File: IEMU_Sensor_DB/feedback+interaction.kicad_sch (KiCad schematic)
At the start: 29 parts, among them J301 +, J302 -, M401 VZ43FM1B8230001L, Q301 CSD13381F4, Q302 CSD13381F4, Q303 CSD13381F4, Q304 CSD13381F4, SW301 NANOT_160_BP, SW302 TS-1088-AR02016

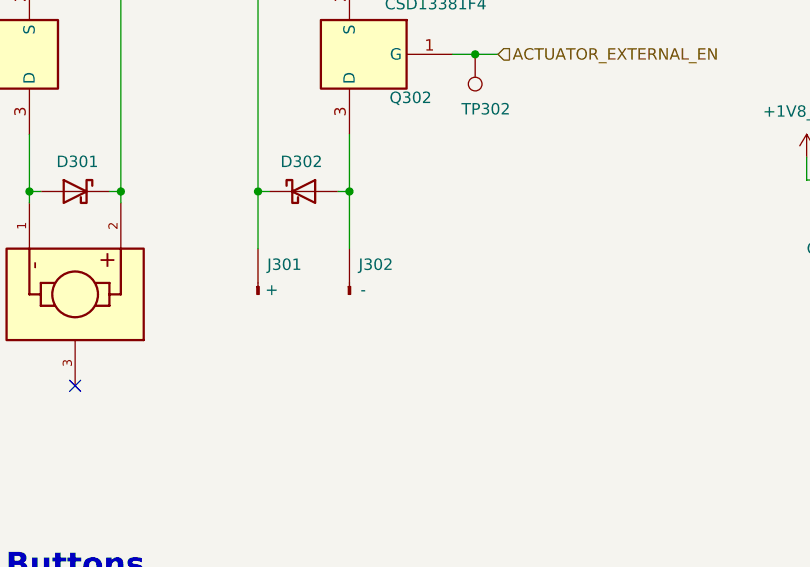
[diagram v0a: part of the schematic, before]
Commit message: swapped the coin cell vibration actuator pins
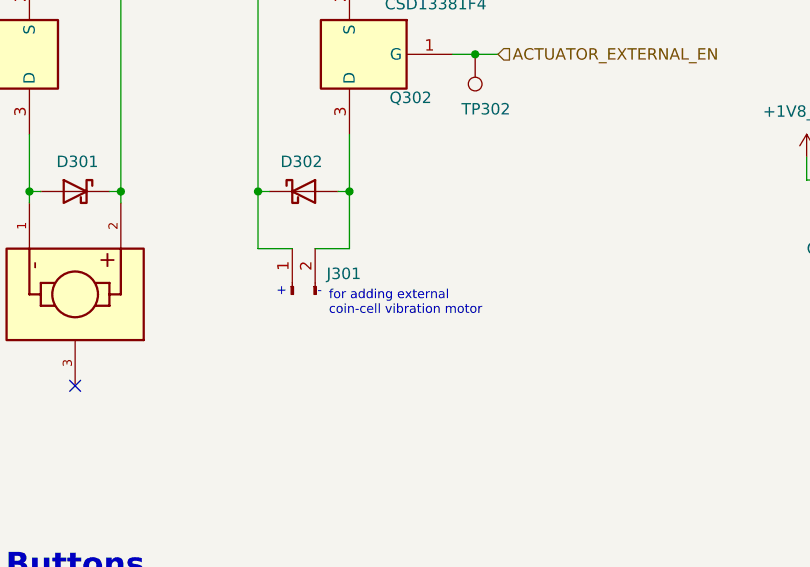
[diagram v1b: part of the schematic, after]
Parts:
- removed J301: +, 0_Connectors:Edge_Header_Pin, symbol 0_Connectors:Connector_Pin_Header_Edge
- removed J302: -, 0_Connectors:Edge_Header_Pin, symbol 0_Connectors:Connector_Pin_Header_Edge
- added J301: Conn_01x02_Pin, Connector_Wire:SolderWire-0.5sqmm_1x02_P4.6mm_D0.9mm_OD2.1mm, symbol Connector:Conn_01x02_Pin
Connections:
- net +3V0: now also J301.1 (Pin_1)
- net at D302.2 (A), Q302.3 (D): now also J301.2 (Pin_2)
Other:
- note added: "+"
- note added: "-"
- note added: "for adding external coin-cell vibration motor"
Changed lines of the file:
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@@
 		)
 	)
+	(text "+"
+		(exclude_from_sim no)
+		(at 82.042 115.316 0)
+		(effects
+			(font
+				(size 1.016 1.016)
+			)
+			(justify left)
+		)
+	)
 	(text "Actuators, LEDs & Buttons"
 		(exclude_from_sim no)
@@
 		)
 	)
+	(text "-"
+		(exclude_from_sim no)
+		(at 86.614 115.316 0)
+		(effects
+			(font
+				(size 1.016 1.016)
+			)
+			(justify left)
+		)
+	)
 	(text "+VSYS Rail"
 		(exclude_from_sim no)
@@
 		)
 	)
+	(text "for adding external \ncoin-cell vibration motor"
+		(exclude_from_sim no)
+		(at 87.884 116.586 0)
+		(effects
+			(font
+				(size 1.016 1.016)
+			)
+			(justify left)
+		)
+	)
 	(text "Haptic Actuators"
 		(exclude_from_sim no)
@@
 	(wire
 		(pts
+			(xy 86.36 110.49) (xy 90.17 110.49)
+		)
+		(stroke
+			(width 0)
+			(type default)
+		)
+	)
+	(wire
+		(pts
 			(xy 140.97 102.87) (xy 140.97 100.33)
 		)
@@
 	(wire
 		(pts
+			(xy 80.01 110.49) (xy 83.82 110.49)
+		)
+		(stroke
+			(width 0)
+			(type default)
+		)
+	)
+	(wire
+		(pts
 			(xy 237.49 67.31) (xy 237.49 72.39)
 		)
@@
 	)
 	(symbol
-		(lib_name "Connector_Pin_Header_Edge_1")
-		(lib_id "0_Connectors:Connector_Pin_Header_Edge")
-		(at 80.01 115.57 90)
-		(unit 1)
-		(exclude_from_sim no)
-		(in_bom yes)
-		(on_board yes)
-		(dnp no)
-		(property "Reference" "J301"
-			(at 81.026 112.268 90)
-			(effects
-				(font
-					(size 1.27 1.27)
-				)
-				(justify right)
-			)
-		)
-		(property "Value" "+"
-			(at 81.534 115.062 90)
-			(effects
-				(font
-					(size 1.27 1.27)
-				)
-			)
-		)
-		(property "Footprint" "0_Connectors:Edge_Header_Pin"
-			(at 81.534 115.57 0)
-			(effects
-				(font
-					(size 1.27 1.27)
-				)
-				(hide yes)
-			)
-		)
-		(property "Datasheet" ""
-			(at 85.852 115.57 0)
-			(effects
-				(font
-					(size 1.27 1.27)
-				)
-				(hide yes)
-			)
-		)
-		(property "Description" "Header Pin located on the edge of the board"
-			(at 84.074 115.316 0)
-			(effects
-				(font
-					(size 1.27 1.27)
-				)
-				(hide yes)
-			)
-		)
-		(pin "1"
-		)
-		(instances
-			(project "IEMU"
-				(path "/114b31f2-6a4f-42ef-aa97-5a200e091126/bedc77cc-dda1-48b8-87d2-cdf0a97ca477"
-					(reference "J301")
-					(unit 1)
-				)
-			)
-		)
-	)
-	(symbol
 		(lib_id "0_Feedback:TS-1088-AR02016")
 		(at 113.03 160.02 0)
@@
 	)
 	(symbol
-		(lib_id "0_Connectors:Connector_Pin_Header_Edge")
-		(at 90.17 115.57 90)
-		(unit 1)
-		(exclude_from_sim no)
-		(in_bom yes)
-		(on_board yes)
-		(dnp no)
-		(property "Reference" "J302"
-			(at 91.186 112.268 90)
-			(effects
-				(font
-					(size 1.27 1.27)
-				)
-				(justify right)
-			)
-		)
-		(property "Value" "-"
-			(at 91.694 115.062 90)
-			(effects
-				(font
-					(size 1.27 1.27)
-				)
-			)
-		)
-		(property "Footprint" "0_Connectors:Edge_Header_Pin"
-			(at 91.694 115.57 0)
-			(effects
-				(font
-					(size 1.27 1.27)
-				)
-				(hide yes)
-			)
-		)
-		(property "Datasheet" ""
-			(at 96.012 115.57 0)
-			(effects
-				(font
-					(size 1.27 1.27)
-				)
-				(hide yes)
-			)
-		)
-		(property "Description" "Header Pin located on the edge of the board"
-			(at 94.234 115.316 0)
-			(effects
-				(font
-					(size 1.27 1.27)
-				)
-				(hide yes)
-			)
-		)
-		(pin "1"
-		)
-		(instances
-			(project ""
-				(path "/114b31f2-6a4f-42ef-aa97-5a200e091126/bedc77cc-dda1-48b8-87d2-cdf0a97ca477"
-					(reference "J302")
-					(unit 1)
-				)
-			)
-		)
-	)
-	(symbol
 		(lib_id "Connector:TestPoint")
 		(at 52.07 161.29 0)
@@
 					(unit 1)
 				)
+			)
+		)
+	)
+	(symbol
+		(lib_id "Connector:Conn_01x02_Pin")
+		(at 83.82 115.57 90)
+		(unit 1)
+		(exclude_from_sim no)
+		(in_bom no)
+		(on_board yes)
+		(dnp no)
+		(property "Reference" "J301"
+			(at 87.63 113.284 90)
+			(effects
+				(font
+					(size 1.27 1.27)
+				)
+				(justify right)
+			)
+		)
+		(property "Value" "Conn_01x02_Pin"
+			(at 87.63 116.2049 90)
+			(effects
+				(font
+					(size 1.27 1.27)
+				)
+				(justify right)
+				(hide yes)
+			)
+		)
+		(property "Footprint" "Connector_Wire:SolderWire-0.5sqmm_1x02_P4.6mm_D0.9mm_OD2.1mm"
+			(at 83.82 115.57 0)
+			(effects
+				(font
+					(size 1.27 1.27)
+				)
+				(hide yes)
+			)
+		)
+		(property "Datasheet" "~"
+			(at 83.82 115.57 0)
+			(effects
+				(font
+					(size 1.27 1.27)
+				)
+				(hide yes)
+			)
+		)
+		(property "Description" "Generic connector, single row, 01x02, script generated"
+			(at 83.82 115.57 0)
+			(effects
+				(font
+					(size 1.27 1.27)
+				)
+				(hide yes)
+			)
+		)
+		(pin "2"
+		)
+		(pin "1"
+		)
+		(instances
+			(project ""
+				(path "/114b31f2-6a4f-42ef-aa97-5a200e091126/bedc77cc-dda1-48b8-87d2-cdf0a97ca477"
+					(reference "J301")
+					(unit 1)
+				)

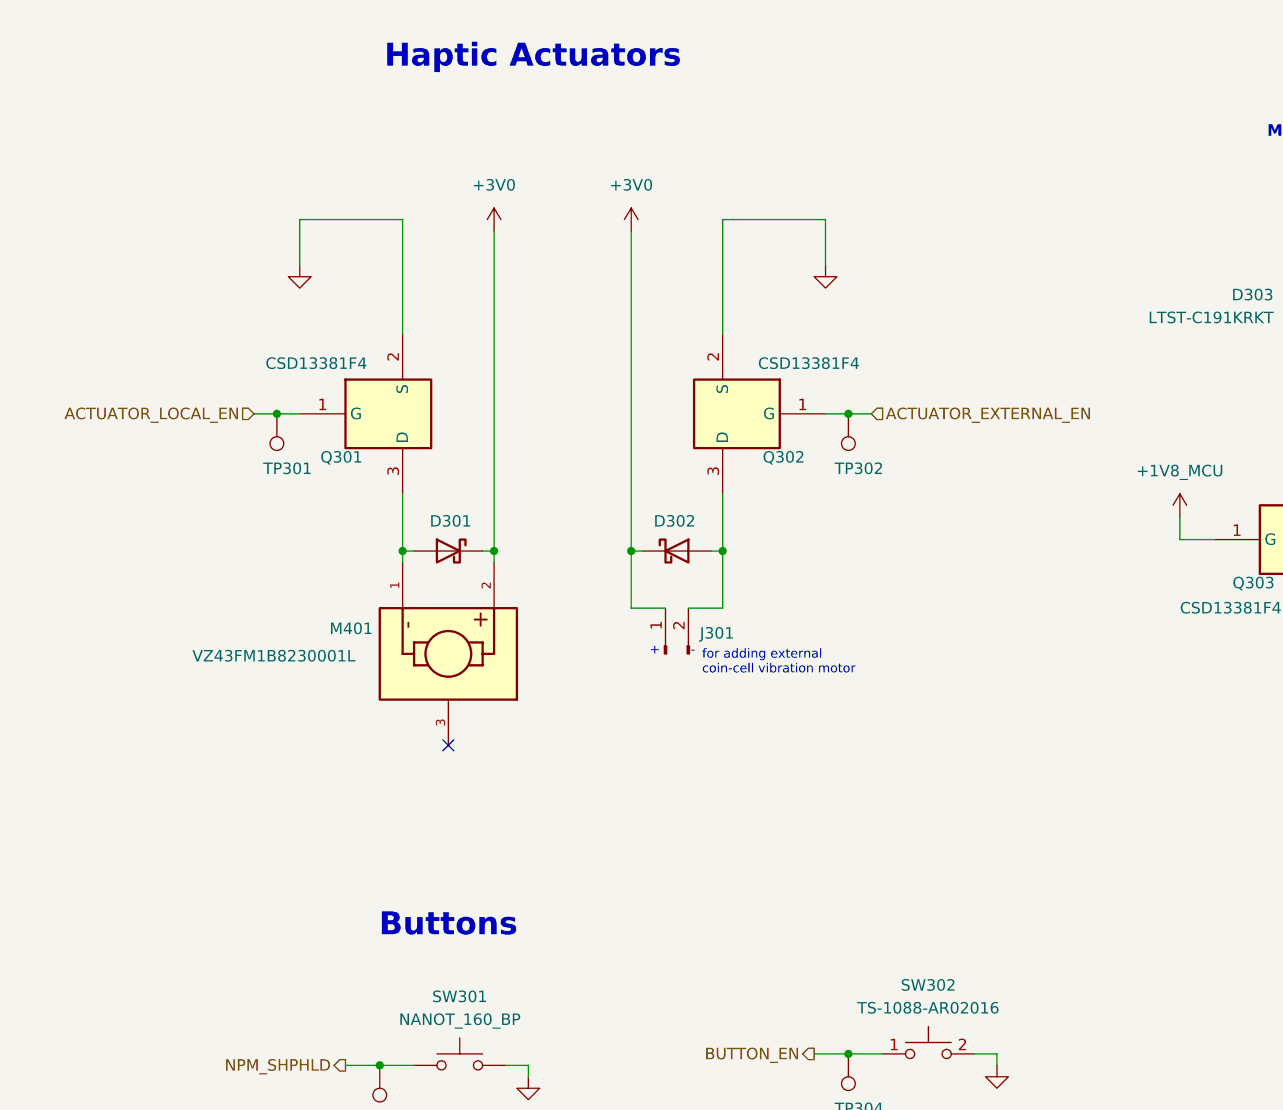
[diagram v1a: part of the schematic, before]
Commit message: implemented changes from the review with TF and fixed lost parts in the library
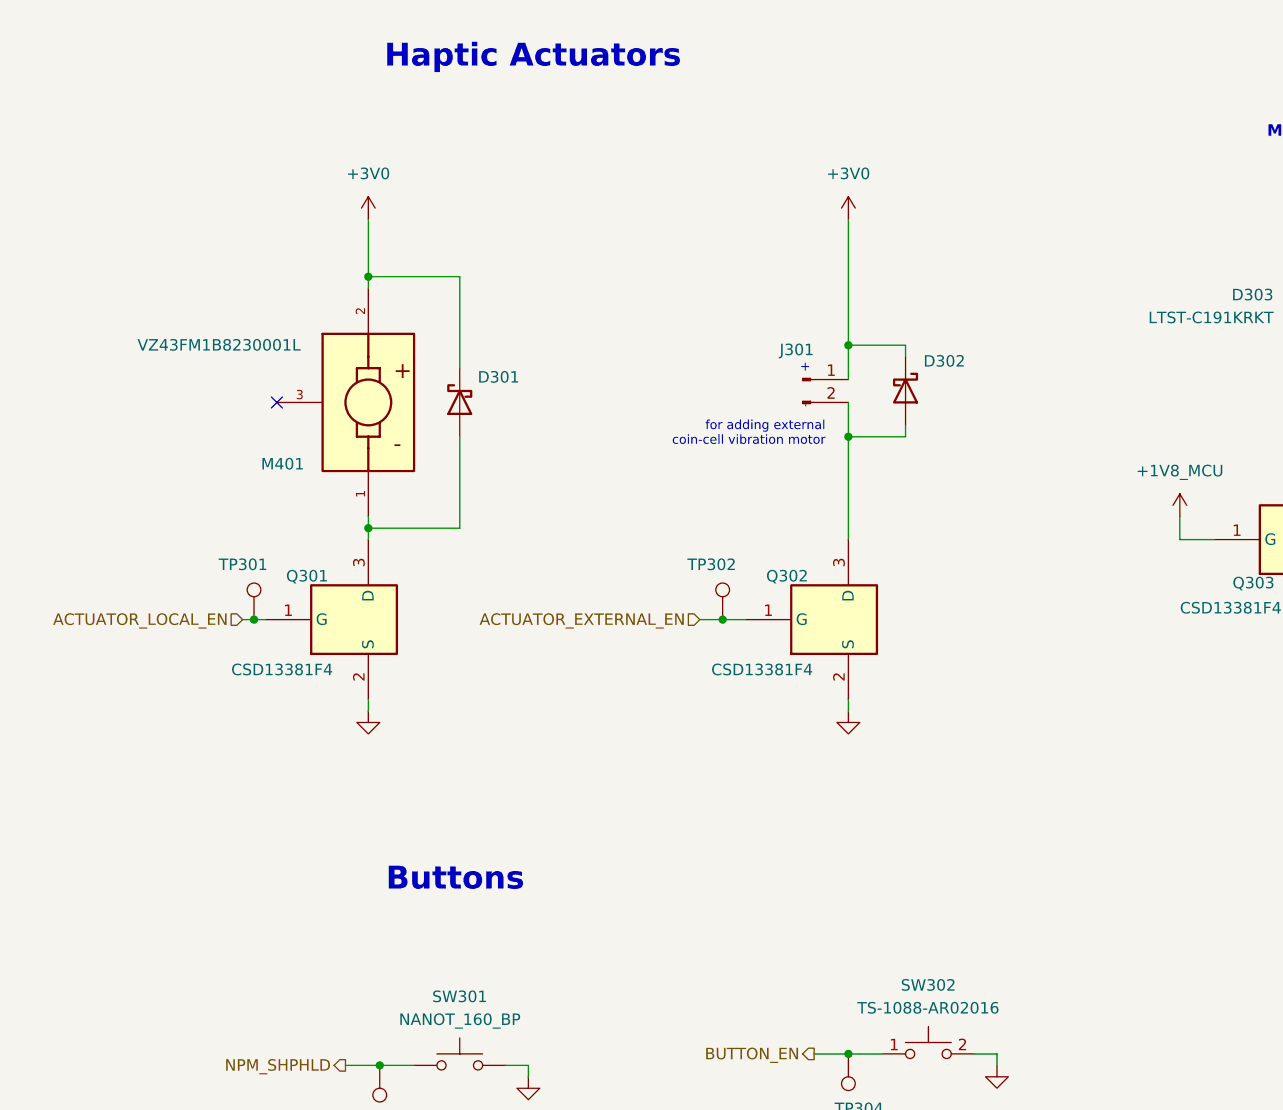
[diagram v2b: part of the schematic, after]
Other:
- moved on the sheet: D301, D302, J301, M401, Q301, Q302, TP301, TP302

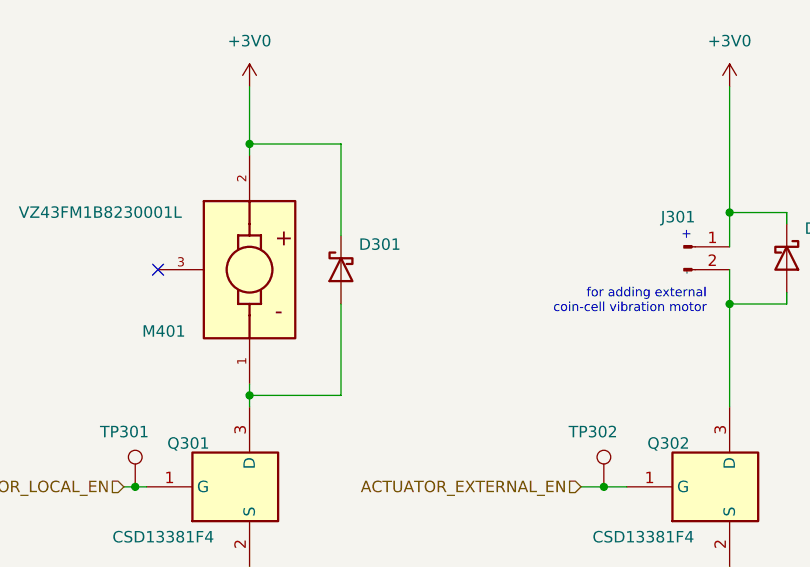
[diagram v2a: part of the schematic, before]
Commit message: finished schematic revision based on TF-review by implementing sensor schematic too
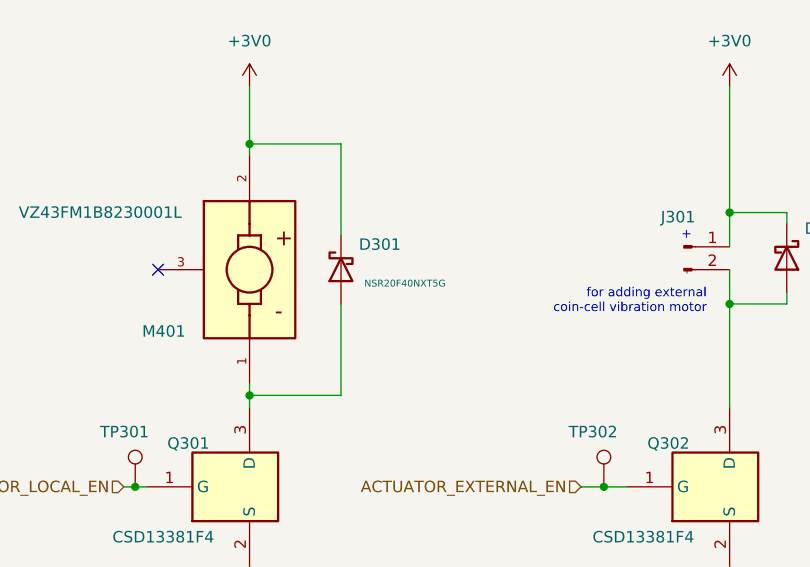
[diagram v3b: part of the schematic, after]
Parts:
- D301, D302: Distributor Link 1 (none) -> https://www.mouser.de/ProductDetail/onsemi/NSR20F40NXT5G?qs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; Distributor Link 2 (none) -> https://www.digikey.de/de/products/detail/onsemi/NSR20F40NX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; LCSC (none) -> C153761; Manufactuer_Name onsemi -> (none); Manufacturer_Name (none) -> onsemi

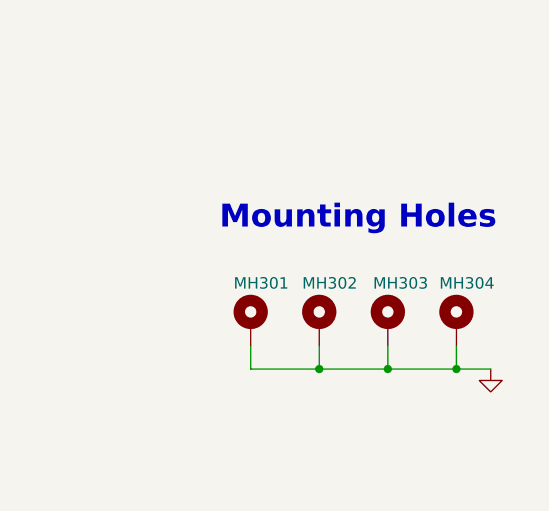
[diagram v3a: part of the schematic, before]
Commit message: created the layout for the sensor (not finished)
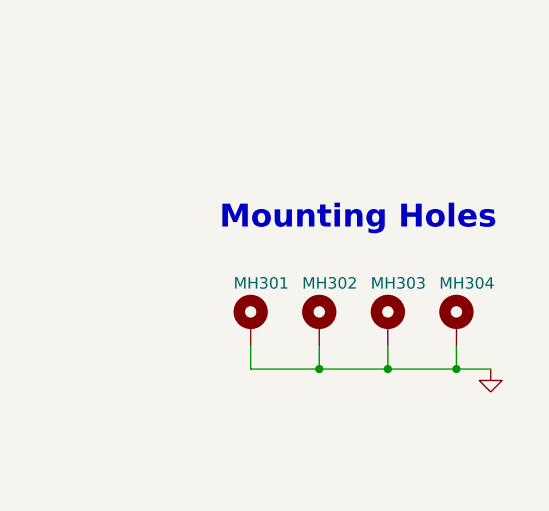
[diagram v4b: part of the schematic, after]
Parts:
- MH301, MH302, MH303, MH304: footprint (none) -> MountingHole:MountingHole_2.2mm_M2_Pad_Via
- TP301, TP302, TP303, TP304: footprint TestPoint:TestPoint_Pad_D2.0mm -> TestPoint:TestPoint_Pad_D1.0mm
